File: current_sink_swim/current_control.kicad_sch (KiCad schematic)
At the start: 8 parts, among them J4 Conn_01x01_Pin, Q1 IRF530NPBF, U1 LMV358

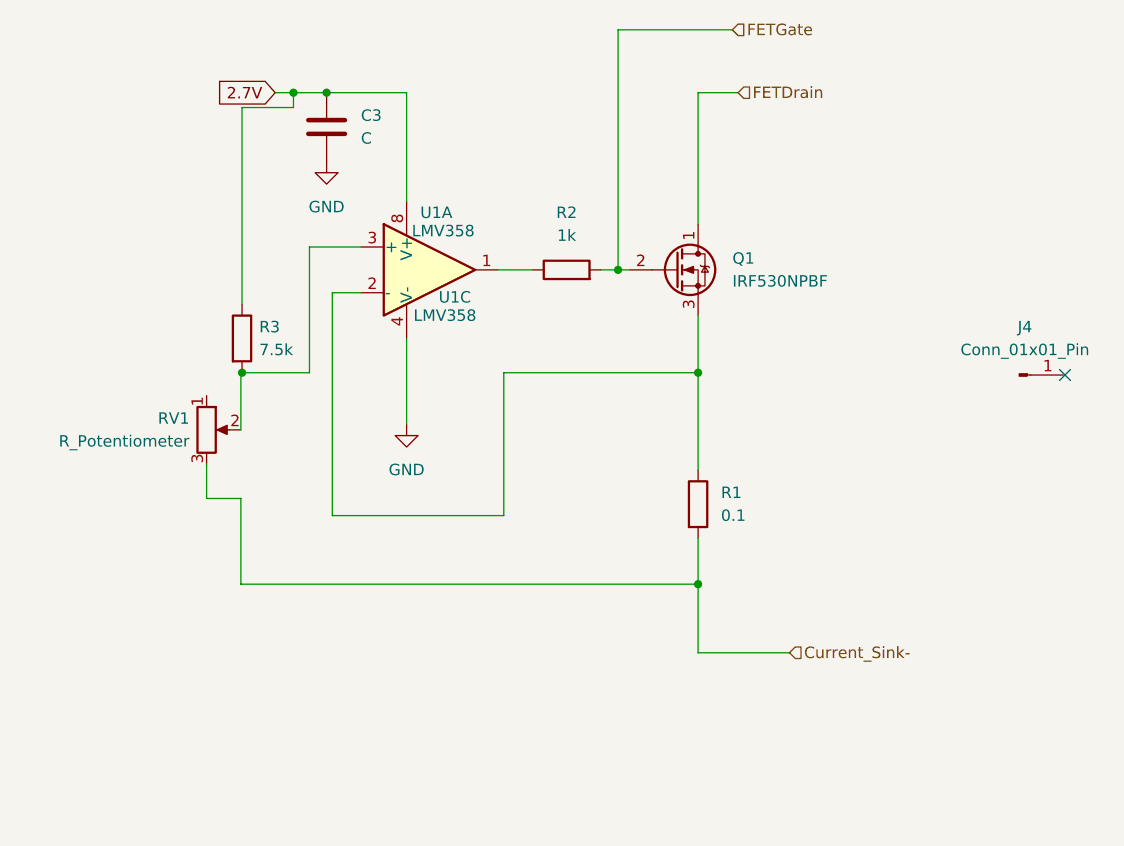
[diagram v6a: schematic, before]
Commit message: first attempt at layout. Probably will be ripped up
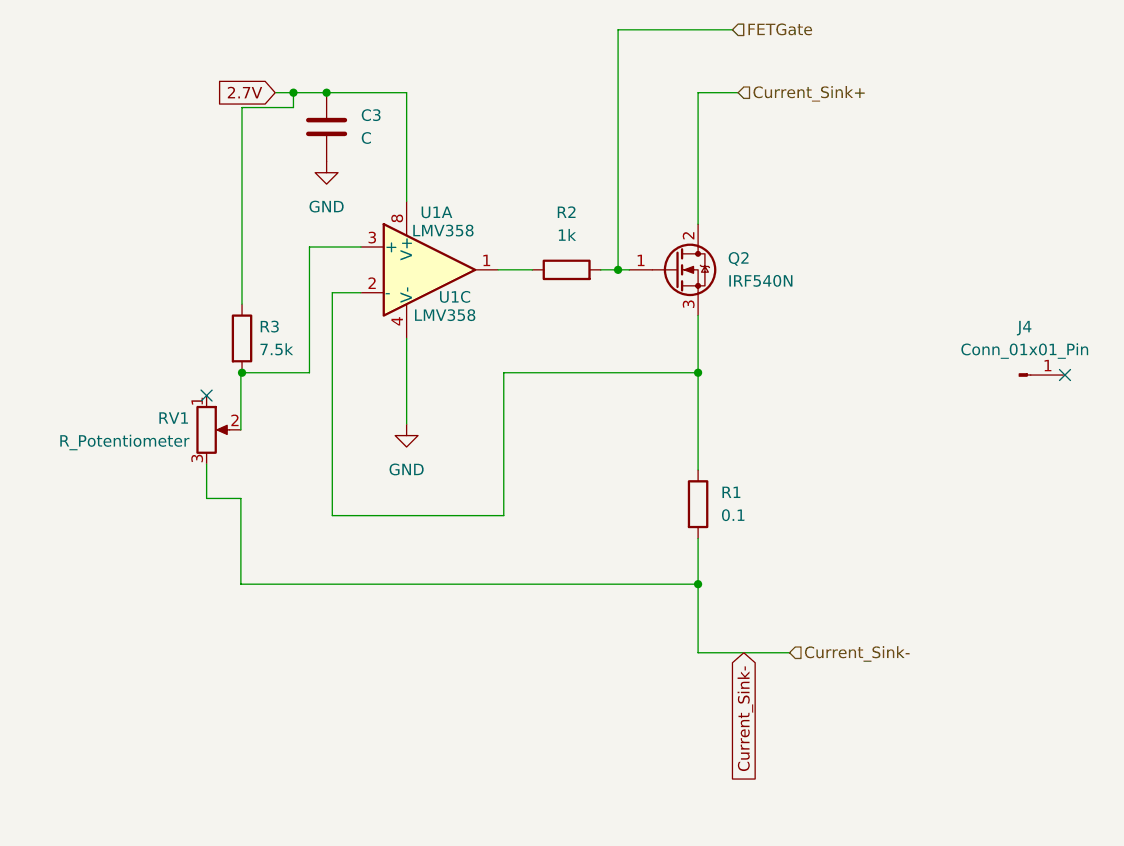
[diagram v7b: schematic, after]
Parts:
- removed Q1: IRF530NPBF, Package_TO_SOT_THT:TO-220-3_Vertical, symbol Device:Q_NMOS_DGS
- added Q2: IRF540N, Package_TO_SOT_THT:TO-220-3_Vertical, symbol Transistor_FET:IRF540N
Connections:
- net FETGate: now also Q2.1 (G)
- net at R1.1, U1.2 (-): now also Q2.3 (S)
- new net Current_Sink+: Q2.2 (D)
- no-connect marks 1 -> 2
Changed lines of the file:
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@@
   (junction (at 123.19 67.945) (diameter 0) (color 0 0 0 0)
   )
+  (no_connect (at 109.855 101.6))
   (no_connect (at 205.232 99.314))
   (wire (pts (xy 153.67 87.63) (xy 155.575 87.63))
@@
     (stroke (width 0) (type default))
   )
+  (wire (pts (xy 119.507 67.945) (xy 123.19 67.945))
+    (stroke (width 0) (type default))
+  )
   (wire (pts (xy 113.792 69.596) (xy 119.507 69.596))
     (stroke (width 0) (type default))
   )
-  (wire (pts (xy 119.507 67.945) (xy 123.19 67.945))
-    (stroke (width 0) (type default))
-  )
   (wire (pts (xy 164.465 67.945) (xy 168.91 67.945))
     (stroke (width 0) (type default))
@@
   (wire (pts (xy 119.507 69.596) (xy 119.507 67.945))
     (stroke (width 0) (type default))
+  )
+  (global_label "Current_Sink-" (shape input) (at 169.545 130.175 270) (fields_autoplaced)
+    (effects (font (size 1.27 1.27)) (justify right))
+    (property "Intersheetrefs" "${INTERSHEET_REFS}" (at 169.545 146.6463 90)
+      (effects (font (size 1.27 1.27)) (justify right) hide)
+    )
   )
   (global_label "2.7V" (shape input) (at 117.475 67.945 180) (fields_autoplaced)
@@
     )
   )
-  (hierarchical_label "FETDrain" (shape input) (at 168.91 67.945 0) (fields_autoplaced)
+  (hierarchical_label "Current_Sink+" (shape input) (at 168.91 67.945 0) (fields_autoplaced)
     (effects (font (size 1.27 1.27)) (justify left))
   )
@@
     )
   )
+  (symbol (lib_id "Transistor_FET:IRF540N") (at 161.925 87.63 0) (unit 1)
+    (in_bom yes) (on_board yes) (dnp no) (fields_autoplaced)
+    (property "Reference" "Q2" (at 167.767 86.36 0)
+      (effects (font (size 1.27 1.27)) (justify left))
+    )
+    (property "Value" "IRF540N" (at 167.767 88.9 0)
+      (effects (font (size 1.27 1.27)) (justify left))
+    )
+    (property "Footprint" "Package_TO_SOT_THT:TO-220-3_Vertical" (at 168.275 89.535 0)
+      (effects (font (size 1.27 1.27) italic) (justify left) hide)
+    )
+    (property "Datasheet" "http://www.irf.com/product-info/datasheets/data/irf540n.pdf" (at 161.925 87.63 0)
+      (effects (font (size 1.27 1.27)) (justify left) hide)
+    )
+    (pin "1")
+    (pin "2")
+    (pin "3")
+    (instances
+      (project "current_sink_swim"
+        (path "/d8f9bd22-1078-406d-bafe-f69bb2710c23/7bb47634-abd5-40f7-90e5-fb54860f3e74"
+          (reference "Q2") (unit 1)
+        )
+      )
+    )
+  )
   (symbol (lib_id "Amplifier_Operational:LMV358") (at 134.62 87.63 0) (unit 1)
     (in_bom yes) (on_board yes) (dnp no)
@@
         )
       )
-    )
-  )
-  (symbol (lib_id "Device:Q_NMOS_DGS") (at 161.925 87.63 0) (unit 1)
-    (in_bom yes) (on_board yes) (dnp no) (fields_autoplaced)
-    (property "Reference" "Q1" (at 168.275 86.36 0)
-      (effects (font (size 1.27 1.27)) (justify left))
-    )
-    (property "Value" "IRF530NPBF" (at 168.275 88.9 0)
-      (effects (font (size 1.27 1.27)) (justify left))
-    )
-    (property "Footprint" "Package_TO_SOT_THT:TO-220-3_Vertical" (at 167.005 85.09 0)
-      (effects (font (size 1.27 1.27)) hide)
-    )
-    (property "Datasheet" "https://www.infineon.com/dgdl/irf530npbf.pdf?fileId=5546d462533600a4015355e386b1199a" (at 161.925 87.63 0)
-      (effects (font (size 1.27 1.27)) hide)
-    )
-    (property "MPN" "IRF530NPBF" (at 161.925 87.63 0)
-      (effects (font (size 1.27 1.27)) hide)
-    )
-    (pin "1")
-    (pin "2")
-    (pin "3")
-    (instances
-      (project "current_sink_swim"
-        (path "/d8f9bd22-1078-406d-bafe-f69bb2710c23"
-          (reference "Q1") (unit 1)
-        )
-        (path "/d8f9bd22-1078-406d-bafe-f69bb2710c23/7bb47634-abd5-40f7-90e5-fb54860f3e74"
-          (reference "Q1") (unit 1)
-        )
-      )
